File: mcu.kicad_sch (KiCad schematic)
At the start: 38 parts, among them J2 USB-C, J3 UART0, J4 I2C / Qwiic, J5 SPI, J6 WS2812, J7 Spare IO, J8 Rail break-out, SW1 RESET, SW2 BOOT, U4 ESP32-S3-WROOM-1-N16R8, U5 USBLC6-2SC6, U6 74AHCT1G125

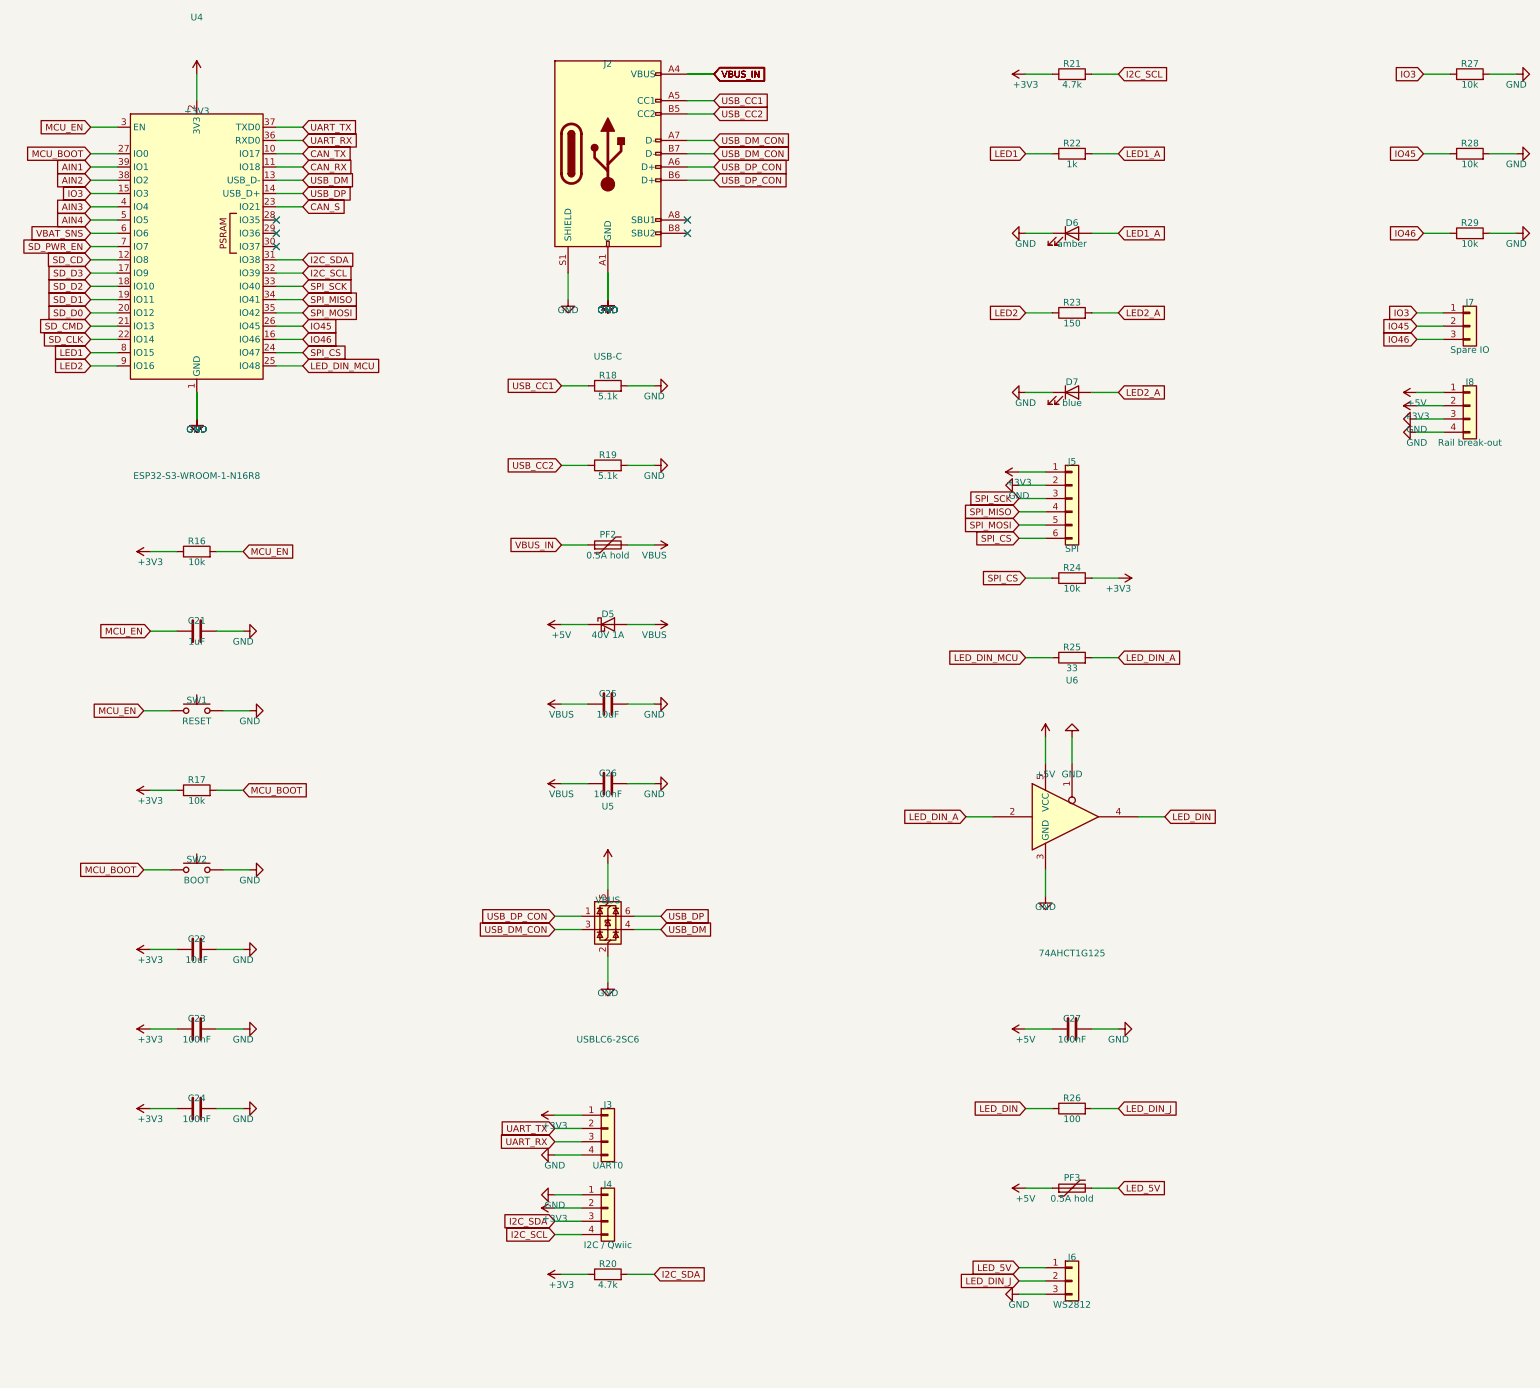
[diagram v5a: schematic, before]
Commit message: Rev B is fully routed: zero DRC errors, nothing unconnected
84 x 84 mm, 1447 tracks, 258 vias, 179 footprints, 106 nets.

The last few connections were never routing problems. Each one was a part
sited away from the net it belongs to, and the autorouter reporting "no
path at any width" was telling the truth:

  +5VS  the sensor rail's source (PF1/FB2/D3) sat on the right beside the
        WS2812 header while everything it feeds -- the sensor harness and
        all four channel pull-ups -- is on the left. The net existed as
        two complete halves with a 45 mm gap through buck islands and the
        SD socket. Moved the source to the harness side.
  IO46  the strapping pull-downs were parked in the bottom band while
        IO3/IO45/IO46 run from the module's south pads to J7 at the top
        left, so R29 needed a trace the length of the board to reach its
        own net. Moved them under the module's south pads.

Adding router passes had never touched either. Moving the parts fixed
both immediately -- worth remembering next time a net "cannot be routed".

Also in this pass:

  - One LED. D6 (amber) and D7 (blue) and their resistors are gone; D4
    green stays on +3V3, which is the right rail to watch because it only
    lights if the whole chain came through -- battery, ideal diode, both
    converters. That also retires review item 11.2.10, the blue emitter
    that would have been near-invisible on a 3.288 V rail.
  - J7 grows to six pins: the three strapping pins, the two GPIOs freed
    by the LEDs (IO15/IO16), and a ground pin. The missing ground was
    review item 13.4.13.
  - USB_CC1 gets a Fine netclass at 0.2 mm. There is no route at 0.25 mm
    -- the USB-C pads are on 0.5 mm pitch and will not pass it -- and CC
    carries under a milliamp through a 5.1k pull-down.
  - build_board.py takes a lock. Two builds sharing the board file is how
    one run died at "Specctra session import failed" after ten minutes,
    when a second build regenerated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
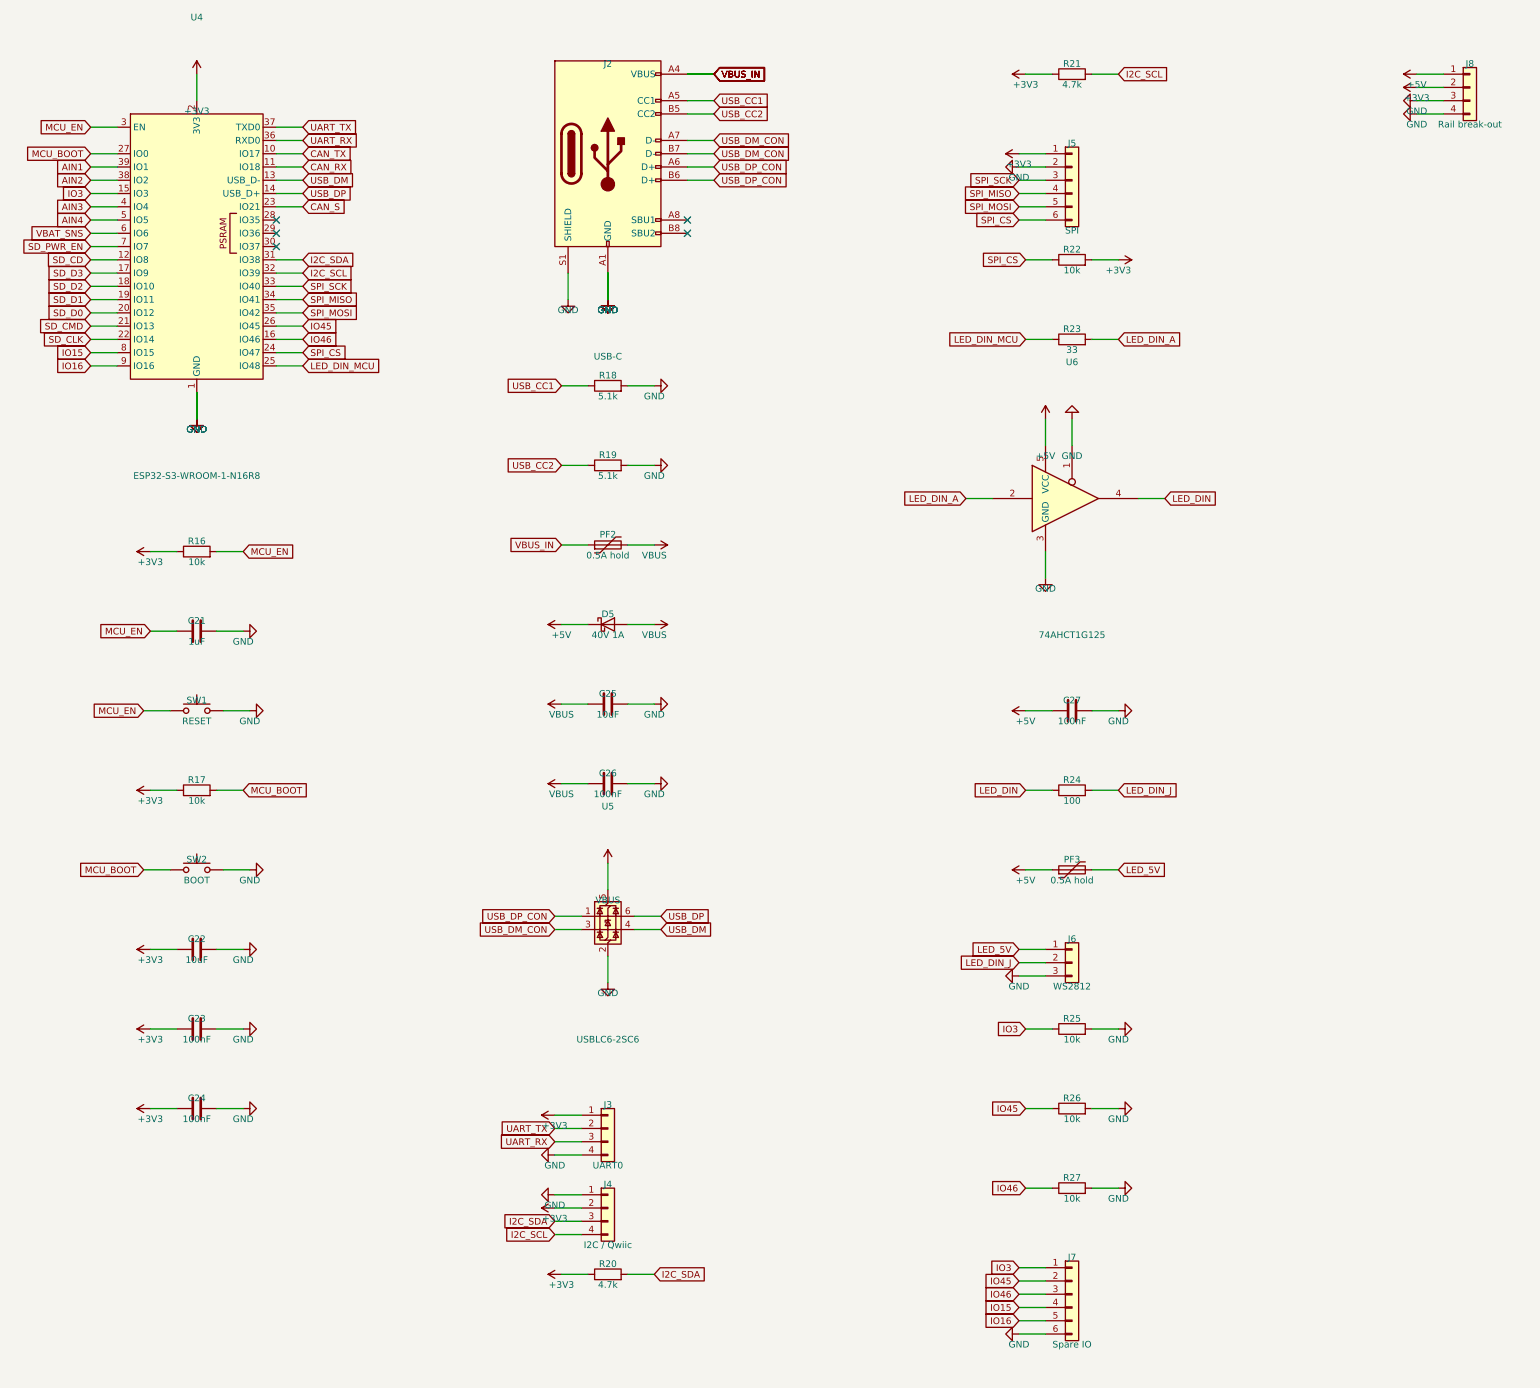
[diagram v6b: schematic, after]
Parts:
- removed D6: amber, LED_SMD:LED_0805_2012Metric, symbol Device:LED
- removed D7: blue, LED_SMD:LED_0805_2012Metric, symbol Device:LED
- removed R28, R29: 10k, Resistor_SMD:R_0805_2012Metric, symbol Device:R
- J7: footprint Connector_PinHeader_2.54mm:PinHeader_1x03_P2.54mm_Vertical -> Connector_PinHeader_2.54mm:PinHeader_1x06_P2.54mm_Vertical; symbol Connector_Generic:Conn_01x03 -> Connector_Generic:Conn_01x06; Note IO3/IO45/IO46 are strapping pins, each with a 10k pull-down. Anything attached must not fight it at boot -> IO3/IO45/IO46 are strapping pins, each with a 10k pull-down -- anything attached must not fight them at boot. IO15/IO16 are ordinary GPIOs, free since the status LEDs came off. The ground pin is here so a probe or a ribbon has a return
- R22: value 1k -> 10k; Note (none) -> Holds an attached slave deselected until firmware drives IO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
- R23: value 150 -> 33; Note Blue Vf sits close to 3.288V, so 1k here gave about 0.19mA 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 -> Edge-rate limit into the level shifter
- R24: value 10k -> 100; Note Holds an attached slave deselected until firmware drives IO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 -> Series termination into the strip. The buffer drove the con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
- R25: value 33 -> 10k; Note Edge-rate limit into the level shifter -> Strapping pin held low at boot
- R26: value 100 -> 10k; Note Series termination into the strip. The buffer drove the con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 -> Strapping pin: VDD_SPI = 3.3V
- R27: Note Strapping pin held low at boot -> Strapping pin: normal boot mode
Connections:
- net LED1_A is gone; now on net +3V3: R22.2
- net LED2_A is gone; now on net LED_DIN_A: R23.2
- net +3V3: no longer R24.2
- net GND: now also J7.6 (Pin_6), R25.2, R26.2
- net IO3: now also R25.1; no longer R27.1
- net IO45: now also R26.1
- net IO46: now also R27.1
- net LED_DIN: now also R24.1; no longer R26.1
- net LED_DIN_A: no longer R25.2
- net LED_DIN_J: now also R24.2; no longer R26.2
- net LED_DIN_MCU: now also R23.1; no longer R25.1
- net SPI_CS: now also R22.1; no longer R24.1
- net LED1 renamed IO15
- net IO15: now also J7.4 (Pin_4); no longer R22.1
- net LED2 renamed IO16
- net IO16: now also J7.5 (Pin_5); no longer R23.1
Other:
- moved on the sheet: C27, J5, J6, J8, PF3, R22, R23, R24, R25, R27, U6
